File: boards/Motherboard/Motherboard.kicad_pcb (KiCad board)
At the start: 2 copper layers, 218 x 122 mm, 161 parts, among them J201 DIGILENT VHDCI, J601 USB, P601 ICSP, P602 SPI2, U401 24AA014, U501 ROE-0505S, U601 SI8660, U602 SI8660, U603 SI8660, U604 SI8660, U605 SI8630/SI8660, U606 SI8630/SI8660, U607 PIC18F85J94, U608 AAT3221IGV-3.3-T1, X601 XTAL, X701 SLOT 1, X702 SLOT 2, X703 SLOT 3, X704 SLOT 4, X705 SLOT 5

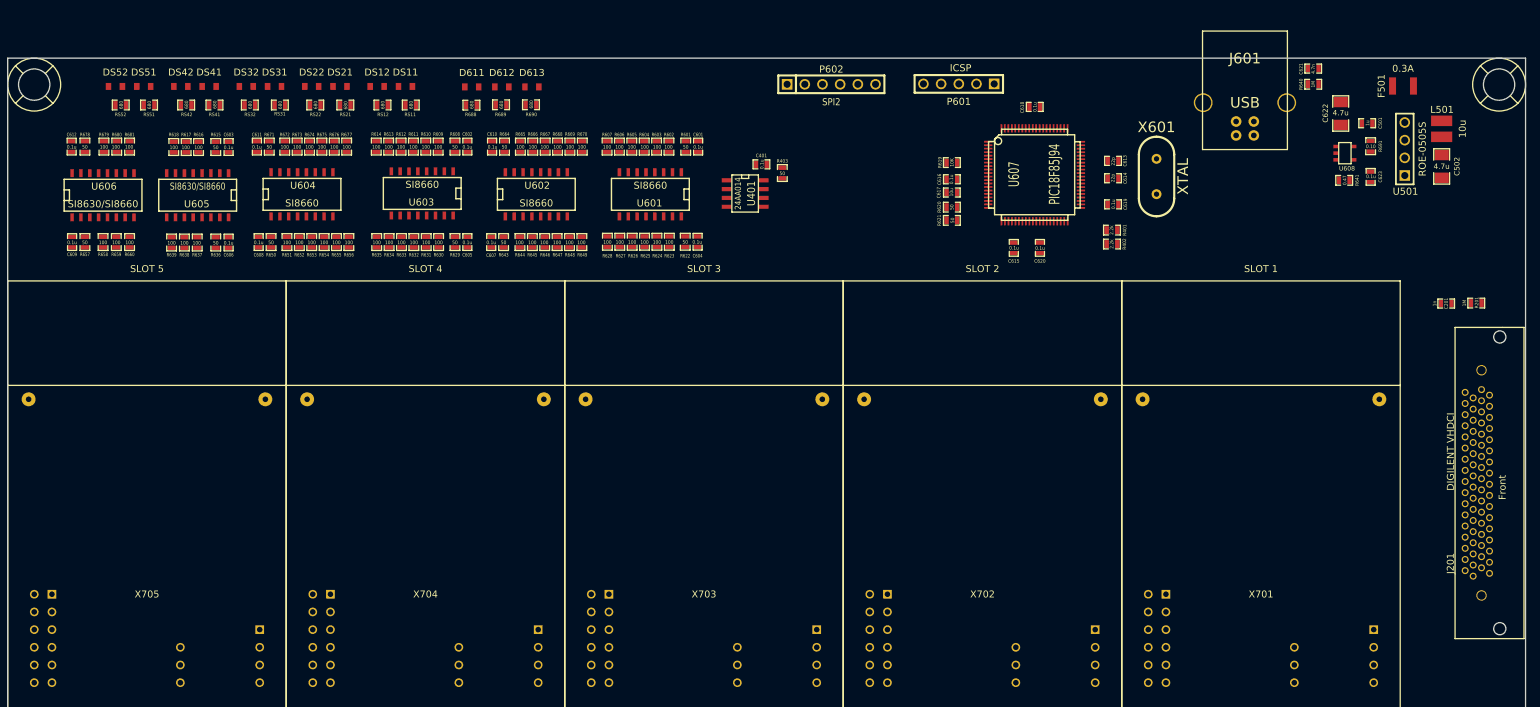
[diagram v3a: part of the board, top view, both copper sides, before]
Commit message: Motherboard PCB components arranged within 2 slot area, drawn a dashed line
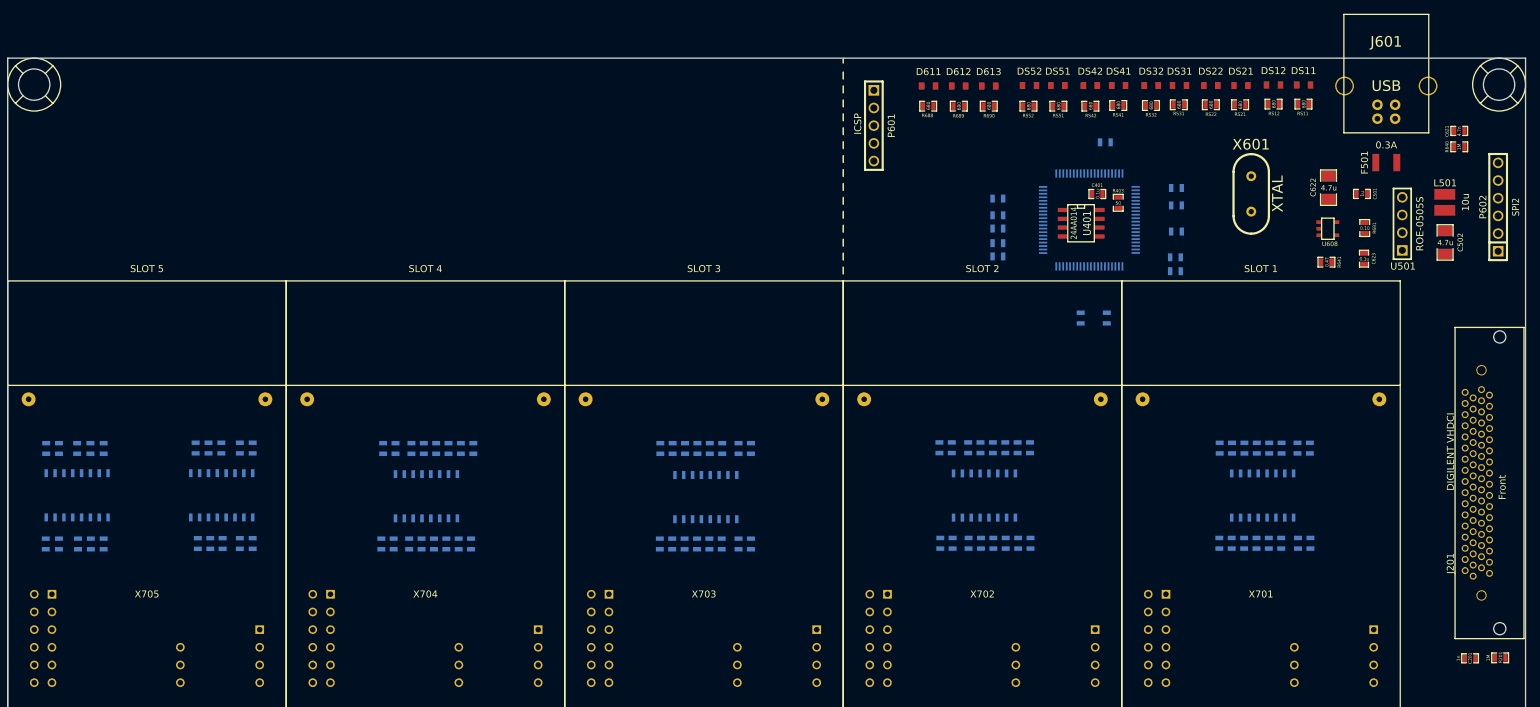
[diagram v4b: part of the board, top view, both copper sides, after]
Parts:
- C601, C602, C603, C604, C605, C606, C607, C608, C609, C610, C611, C612, C613, C614, C615, C616, C617, C618, C619, C620, R401, R402, R601, R602, R603, R604, R605, R606, R607, R608, R609, R610, R611, R612, R613, R614, R615, R616, R617, R618, R619, R620, R621, R622, R623, R624, R625, R626, R627, R628, R629, R630, R631, R632, R633, R634, R635, R636, R637, R638, R639, R643, R644, R645, R646, R647, R648, R649, R650, R651, R652, R653, R654, R655, R656, R657, R658, R659, R660, R664, R665, R666, R667, R668, R669, R670, R671, R672, R673, R674, R675, R676, R677, R678, R679, R680, R681, U601, U602, U603, U604, U605, U606, U607: moved to B.Cu
- moved DS51 131.3 mm to (194.8, 38.9)
- moved DS52 131.3 mm to (190.8, 38.9)
- moved DS41 130.6 mm to (203.6, 38.9)
- moved DS42 130.6 mm to (199.5, 38.9)
- moved RS51 130.6 mm to (194.9, 41.9)
- moved RS52 130.4 mm to (190.6, 41.9)
- moved DS31 130.0 mm to (212.3, 38.9)
- moved DS32 130.0 mm to (208.2, 38.9)
- moved RS42 129.9 mm to (199.5, 41.9)
- moved RS41 129.8 mm to (203.5, 41.8)
- moved RS32 129.4 mm to (208.2, 41.8)
- moved DS21 129.4 mm to (221.1, 38.9)
- moved DS22 129.1 mm to (216.8, 38.9)
- moved RS31 129.1 mm to (212.2, 41.7)
- moved DS11 129.0 mm to (230.1, 38.9)
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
